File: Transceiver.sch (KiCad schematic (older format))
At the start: 31 parts, among them U2 CC1125, U3 BALF-112X-02D3, U4 SKY13372-467LF, X1 KT2520K40000DAW18TAS

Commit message: project files till workbut names are messed up
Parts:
- C19: footprint (none) -> Capacitors_SMD:C_0201
- C20, C21: footprint (none) -> Capacitors_SMD:C_0402
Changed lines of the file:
@@
 F 0 "C19" V 7550 3800 50  0000 C CNN
 F 1 "47pF" V 7250 3800 50  0000 C CNN
-F 2 "" H 7438 3650 50  0001 C CNN
+F 2 "Capacitors_SMD:C_0201" H 7438 3650 50  0001 C CNN
 F 3 "" H 7400 3800 50  0000 C CNN
 	1    7400 3800
@@
 F 0 "C20" V 9675 3550 50  0000 C CNN
 F 1 "47pF" V 9975 3550 50  0000 C CNN
-F 2 "" H 9863 3400 50  0001 C CNN
+F 2 "Capacitors_SMD:C_0402" H 9863 3400 50  0001 C CNN
 F 3 "" H 9825 3550 50  0000 C CNN
 	1    9825 3550
@@
 F 0 "C21" V 9675 4050 50  0000 C CNN
 F 1 "47pF" V 9975 4050 50  0000 C CNN
-F 2 "" H 9863 3900 50  0001 C CNN
+F 2 "Capacitors_SMD:C_0402" H 9863 3900 50  0001 C CNN
 F 3 "" H 9825 4050 50  0000 C CNN
 	1    9825 4050

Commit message: fixed filesystem
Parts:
- C14: footprint (none) -> Capacitors_SMD:C_0402
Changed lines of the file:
@@
 F 0 "C14" H 4625 3100 50  0000 L CNN
 F 1 "1.8nF" H 4625 2900 50  0000 L CNN
-F 2 "" H 4638 2850 50  0001 C CNN
+F 2 "Capacitors_SMD:C_0402" H 4638 2850 50  0001 C CNN
 F 3 "" H 4600 3000 50  0000 C CNN
 	1    4600 3000

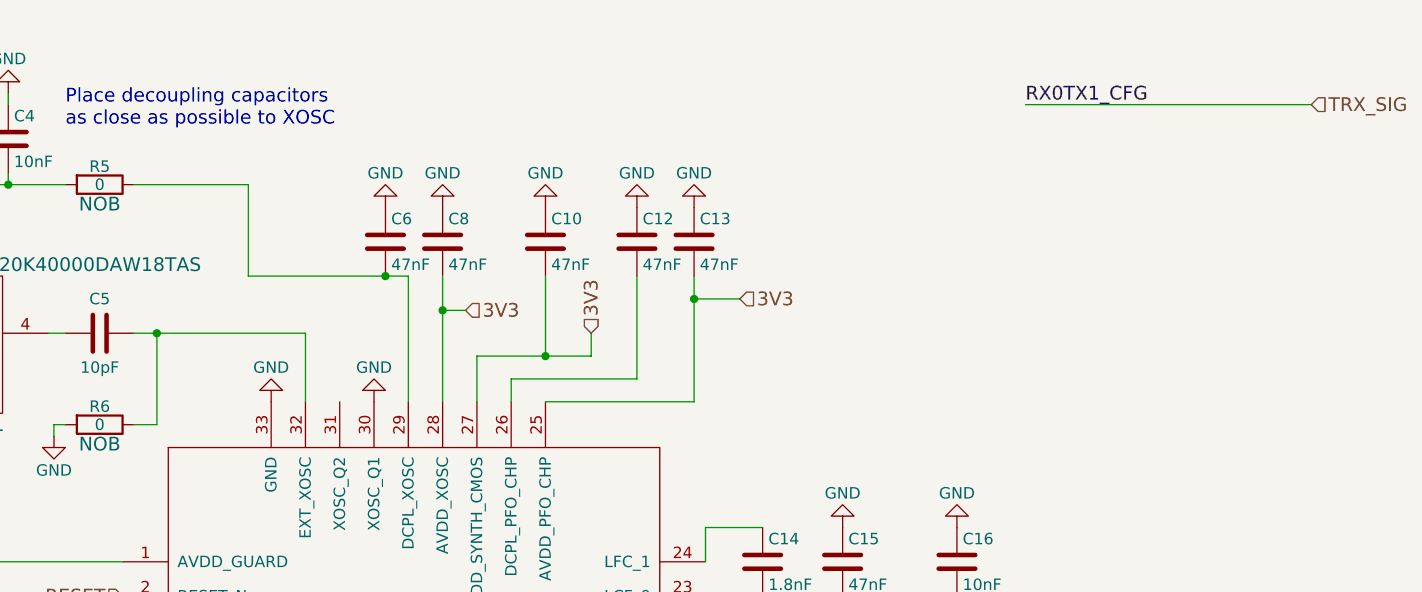
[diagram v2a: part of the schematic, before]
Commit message: added some test points
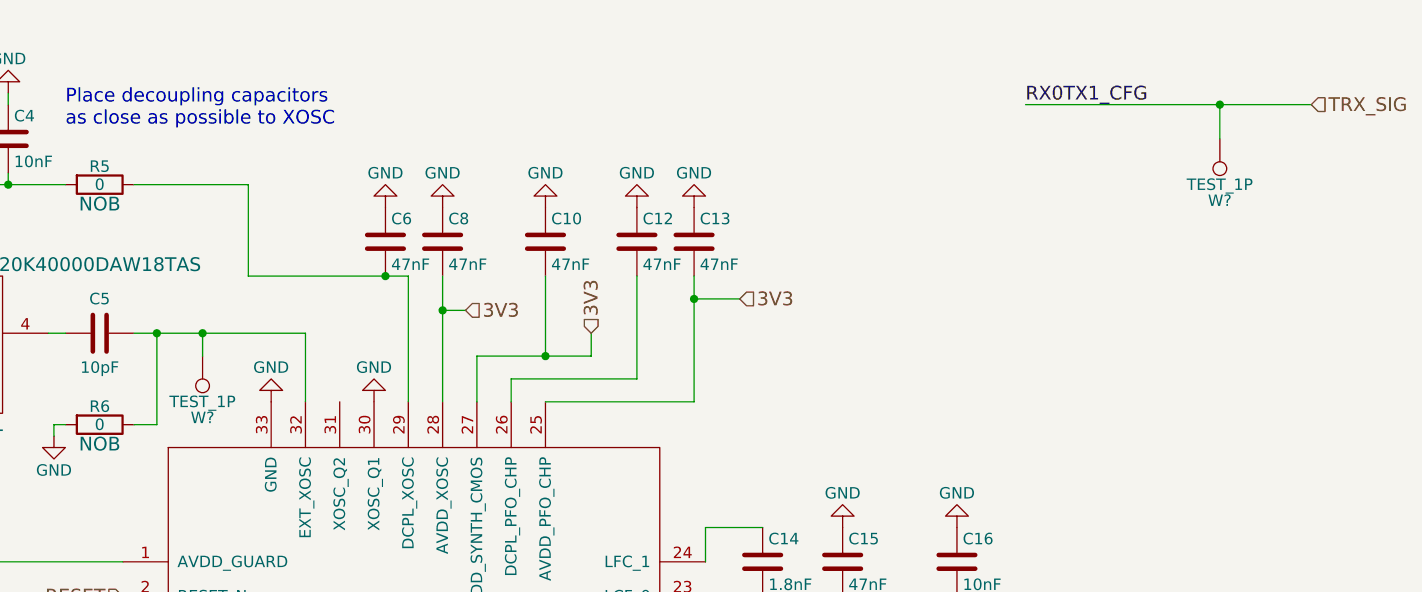
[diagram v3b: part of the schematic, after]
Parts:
- added W? (x2): TEST_1P, symbol TEST_1P
- C19: footprint Capacitors_SMD:C_0201 -> Capacitors_SMD:C_0402
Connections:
- net TRX_SIG: now also W?.1
- net at C5.1, R6.1, U2.32 (EXT_XOSC): now also W?.1
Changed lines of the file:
@@
 F 0 "C19" V 7550 3800 50  0000 C CNN
 F 1 "47pF" V 7250 3800 50  0000 C CNN
-F 2 "Capacitors_SMD:C_0201" H 7438 3650 50  0001 C CNN
+F 2 "Capacitors_SMD:C_0402" H 7438 3650 50  0001 C CNN
 F 3 "" H 7400 3800 50  0000 C CNN
 	1    7400 3800
@@
 Text Label 4800 4050 0    60   ~ 0
 RF_PA
+$Comp
+L TEST_1P W?
+U 1 1 5881B2B5
+P 6600 1150
+F 0 "W?" H 6600 1420 50  0000 C CNN
+F 1 "TEST_1P" H 6600 1350 50  0000 C CNN
+F 2 "" H 6800 1150 50  0000 C CNN
+F 3 "" H 6800 1150 50  0000 C CNN
+	1    6600 1150
+	-1   0    0    1
+$EndComp
+Wire Wire Line
+	6600 1000 6600 1150
+Connection ~ 6600 1000
+$Comp
+L TEST_1P W?
+U 1 1 5881CC09
+P 2150 2100
+F 0 "W?" H 2150 2370 50  0000 C CNN
+F 1 "TEST_1P" H 2150 2300 50  0000 C CNN
+F 2 "" H 2350 2100 50  0000 C CNN
+F 3 "" H 2350 2100 50  0000 C CNN
+	1    2150 2100
+	-1   0    0    1
+$EndComp
+Wire Wire Line
+	2150 2100 2150 2000
+Connection ~ 2150 2000
 $EndSCHEMATC

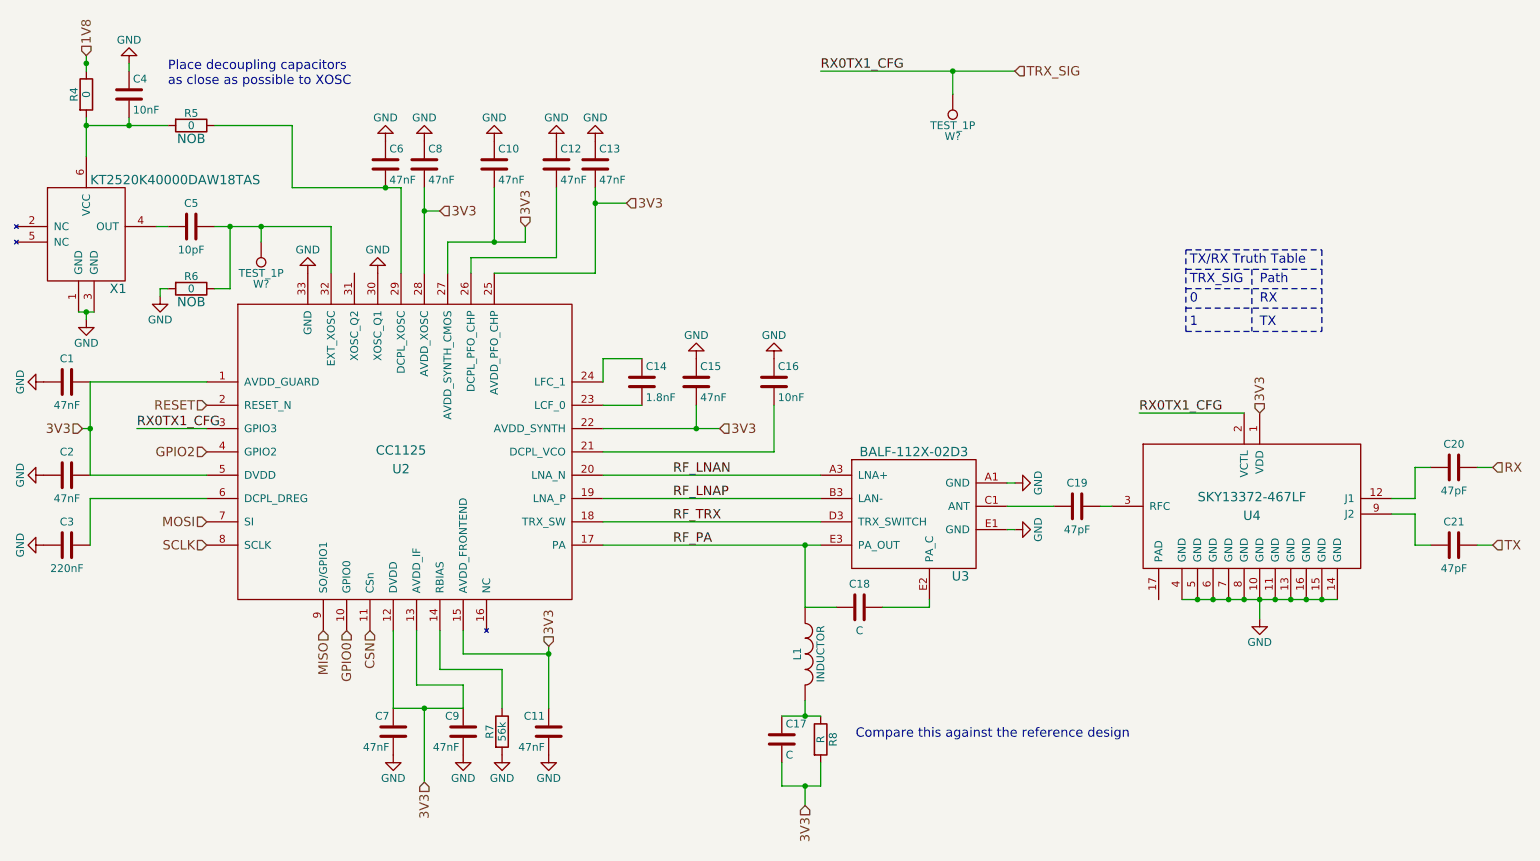
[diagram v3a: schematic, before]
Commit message: layed out all components
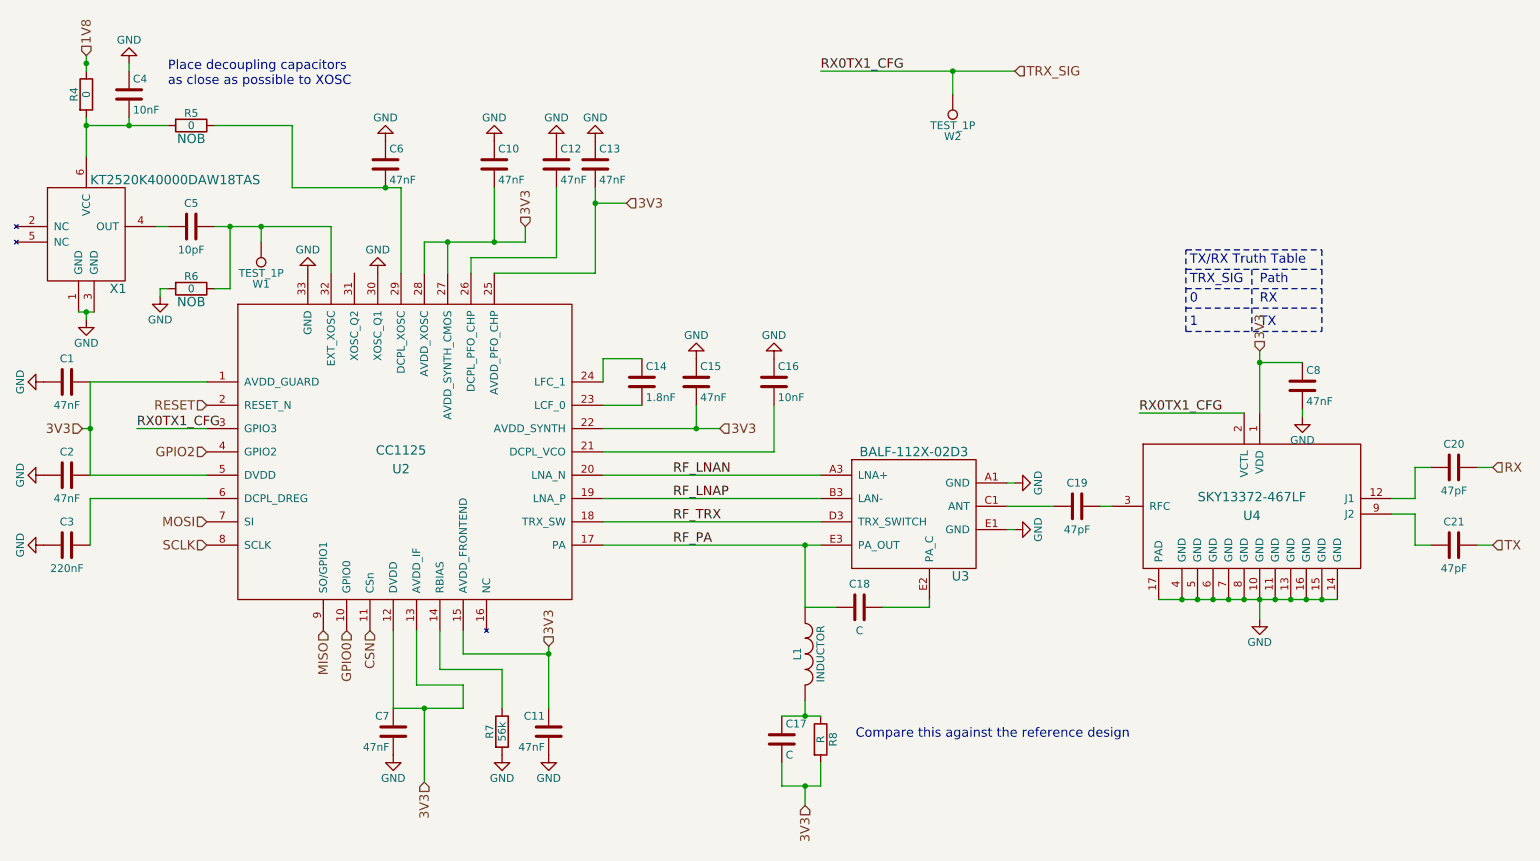
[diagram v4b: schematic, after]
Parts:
- removed C9: 47nF, Capacitors_SMD:C_0402, symbol C
- W1, W2: renamed from W?; footprint (none) -> Measurement_Points:Measurement_Point_Round-SMD-Pad_Small
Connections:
- net 3V3: now also C8.1; no longer C8.2
- net GND: now also C8.2, U4.17 (PAD); no longer C8.1
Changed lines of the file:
@@
-$EndComp
-$Comp
-L C C8
-U 1 1 5821C834
-P 3200 1600
-F 0 "C8" H 3225 1700 50  0000 L CNN
-F 1 "47nF" H 3225 1500 50  0000 L CNN
-F 2 "Capacitors_SMD:C_0402" H 3238 1450 50  0001 C CNN
-F 3 "" H 3200 1600 50  0000 C CNN
-	1    3200 1600
-	1    0    0    -1
-$EndComp
-$Comp
-L GND #PWR09
-U 1 1 5821C83B
-P 3200 1450
-F 0 "#PWR09" H 3200 1200 50  0001 C CNN
-F 1 "GND" H 3200 1300 50  0000 C CNN
-F 2 "" H 3200 1450 50  0000 C CNN
-F 3 "" H 3200 1450 50  0000 C CNN
-	1    3200 1450
-	-1   0    0    1
 $EndComp
 $Comp
@@
 $EndComp
 $Comp
-L GND #PWR010
+L GND #PWR09
 U 1 1 5821C849
 P 3650 1450
-F 0 "#PWR010" H 3650 1200 50  0001 C CNN
+F 0 "#PWR09" H 3650 1200 50  0001 C CNN
 F 1 "GND" H 3650 1300 50  0000 C CNN
 F 2 "" H 3650 1450 50  0000 C CNN
@@
 $EndComp
 $Comp
-L GND #PWR011
+L GND #PWR010
 U 1 1 5821C856
 P 4050 1450
-F 0 "#PWR011" H 4050 1200 50  0001 C CNN
+F 0 "#PWR010" H 4050 1200 50  0001 C CNN
 F 1 "GND" H 4050 1300 50  0000 C CNN
 F 2 "" H 4050 1450 50  0000 C CNN
@@
 $EndComp
 $Comp
-L GND #PWR012
+L GND #PWR011
 U 1 1 5821C863
 P 4300 1450
-F 0 "#PWR012" H 4300 1200 50  0001 C CNN
+F 0 "#PWR011" H 4300 1200 50  0001 C CNN
 F 1 "GND" H 4300 1300 50  0000 C CNN
 F 2 "" H 4300 1450 50  0000 C CNN
@@
 $EndComp
 $Comp
-L GND #PWR013
+L GND #PWR012
 U 1 1 5821C870
 P 2950 1450
-F 0 "#PWR013" H 2950 1200 50  0001 C CNN
+F 0 "#PWR012" H 2950 1200 50  0001 C CNN
 F 1 "GND" H 2950 1300 50  0000 C CNN
 F 2 "" H 2950 1450 50  0000 C CNN
@@
 	1    2950 1450
 	-1   0    0    1
-$EndComp
-$Comp
-L C C9
-U 1 1 5821C876
-P 3450 5250
-F 0 "C9" H 3475 5150 50  0000 L CNN
-F 1 "47nF" H 3475 5350 50  0000 L CNN
-F 2 "Capacitors_SMD:C_0402" H 3488 5100 50  0001 C CNN
-F 3 "" H 3450 5250 50  0000 C CNN
-	1    3450 5250
-	-1   0    0    1
-$EndComp
-$Comp
-L GND #PWR014
-U 1 1 5821C87D
-P 3450 5400
-F 0 "#PWR014" H 3450 5150 50  0001 C CNN
-F 1 "GND" H 3450 5250 50  0000 C CNN
-F 2 "" H 3450 5400 50  0000 C CNN
-F 3 "" H 3450 5400 50  0000 C CNN
-	1    3450 5400
-	1    0    0    -1
 $EndComp
 $Comp
@@
 $EndComp
 $Comp
-L GND #PWR015
+L GND #PWR013
 U 1 1 5821C88A
 P 3000 5400
-F 0 "#PWR015" H 3000 5150 50  0001 C CNN
+F 0 "#PWR013" H 3000 5150 50  0001 C CNN
 F 1 "GND" H 3000 5250 50  0000 C CNN
 F 2 "" H 3000 5400 50  0000 C CNN
@@
 $EndComp
 $Comp
-L GND #PWR016
+L GND #PWR014
 U 1 1 5821C897
 P 4000 5400
-F 0 "#PWR016" H 4000 5150 50  0001 C CNN
+F 0 "#PWR014" H 4000 5150 50  0001 C CNN
 F 1 "GND" H 4000 5250 50  0000 C CNN
 F 2 "" H 4000 5400 50  0000 C CNN
@@
 $EndComp
 $Comp
-L GND #PWR017
+L GND #PWR015
 U 1 1 5821C8A8
 P 3700 5400
-F 0 "#PWR017" H 3700 5150 50  0001 C CNN
+F 0 "#PWR015" H 3700 5150 50  0001 C CNN
 F 1 "GND" H 3700 5250 50  0000 C CNN
 F 2 "" H 3700 5400 50  0000 C CNN
@@
 $EndComp
 $Comp
-L GND #PWR018
+L GND #PWR016
 U 1 1 5821C8BD
 P 4950 2850
-F 0 "#PWR018" H 4950 2600 50  0001 C CNN
+F 0 "#PWR016" H 4950 2600 50  0001 C CNN
 F 1 "GND" H 4950 2700 50  0000 C CNN
 F 2 "" H 4950 2850 50  0000 C CNN
@@
 $EndComp
 $Comp
-L GND #PWR019
+L GND #PWR017
 U 1 1 5821C8CA
 P 5450 2850
-F 0 "#PWR019" H 5450 2600 50  0001 C CNN
+F 0 "#PWR017" H 5450 2600 50  0001 C CNN
 F 1 "GND" H 5450 2700 50  0000 C CNN
 F 2 "" H 5450 2850 50  0000 C CNN
@@
 $EndComp
 $Comp
-L GND #PWR020
+L GND #PWR018
 U 1 1 5821C9D7
 P 2450 2300
-F 0 "#PWR020" H 2450 2050 50  0001 C CNN
+F 0 "#PWR018" H 2450 2050 50  0001 C CNN
 F 1 "GND" H 2450 2150 50  0000 C CNN
 F 2 "" H 2450 2300 50  0000 C CNN
@@
 $EndComp
 $Comp
-L GND #PWR021
+L GND #PWR019
 U 1 1 5821C9E6
 P 2900 2300
-F 0 "#PWR021" H 2900 2050 50  0001 C CNN
+F 0 "#PWR019" H 2900 2050 50  0001 C CNN
 F 1 "GND" H 2900 2150 50  0000 C CNN
 F 2 "" H 2900 2300 50  0000 C CNN
@@
 $EndComp
 $Comp
-L GND #PWR022
+L GND #PWR020
 U 1 1 5821C9FA
 P 1025 2600
-F 0 "#PWR022" H 1025 2350 50  0001 C CNN
+F 0 "#PWR020" H 1025 2350 50  0001 C CNN
 F 1 "GND" H 1025 2450 50  0000 C CNN
 F 2 "" H 1025 2600 50  0000 C CNN
@@
 Text HLabel 1025 900  1    60   Input ~ 0
 1V8
-Text HLabel 3300 1900 2    60   Input ~ 0
-3V3
 Text HLabel 3850 2000 1    60   Input ~ 0
 3V3
@@
 $EndComp
 $Comp
-L GND #PWR023
+L GND #PWR021
 U 1 1 58730157
 P 7000 3650
-F 0 "#PWR023" H 7000 3400 50  0001 C CNN
+F 0 "#PWR021" H 7000 3400 50  0001 C CNN
 F 1 "GND" H 7000 3500 50  0000 C CNN
 F 2 "" H 7000 3650 50  0000 C CNN
@@
 $EndComp
 $Comp
-L GND #PWR024
+L GND #PWR022
 U 1 1 5873019B
 P 7000 3950
-F 0 "#PWR024" H 7000 3700 50  0001 C CNN
+F 0 "#PWR022" H 7000 3700 50  0001 C CNN
 F 1 "GND" H 7000 3800 50  0000 C CNN
 F 2 "" H 7000 3950 50  0000 C CNN
@@
 Text Notes 1550 1100 0    60   ~ 0
 Place decoupling capacitors\nas close as possible to XOSC\n
-Text HLabel 8575 3200 1    60   Input ~ 0
+Text HLabel 8575 2800 1    60   Input ~ 0
 3V3
 $Comp
@@
 	3350 2300 3350 2100
 Wire Wire Line
-	3350 2100 3850 2100
+	3200 2100 3850 2100
 Wire Wire Line
 	3650 2100 3650 1750
@@
 	3850 2100 3850 2000
 Connection ~ 3650 2100
-Wire Wire Line
-	3200 1750 3200 2300
-Wire Wire Line
-	3200 1900 3300 1900
-Connection ~ 3200 1900
 Wire Wire Line
 	3050 1750 3050 2300
@@
 	8525 2275 8525 2675
 $Comp
-L GND #PWR025
+L GND #PWR023
 U 1 1 58748992
 P 8575 4525
-F 0 "#PWR025" H 8575 4275 50  0001 C CNN
+F 0 "#PWR023" H 8575 4275 50  0001 C CNN
 F 1 "GND" H 8575 4375 50  0000 C CNN
 F 2 "" H 8575 4525 50  0000 C CNN
@@
 $EndComp
 Wire Wire Line
-	8075 4400 9075 4400
+	7925 4400 9075 4400
 Connection ~ 8175 4400
 Connection ~ 8275 4400
@@
 	1300 1300 1300 1350
 $Comp
-L GND #PWR026
+L GND #PWR024
 U 1 1 5873A98A
 P 1300 950
-F 0 "#PWR026" H 1300 700 50  0001 C CNN
+F 0 "#PWR024" H 1300 700 50  0001 C CNN
 F 1 "GND" H 1300 800 50  0000 C CNN
 F 2 "" H 1300 950 50  0000 C CNN
@@
 	1500 2400 1500 2450
 $Comp
-L GND #PWR027
+L GND #PWR025
 U 1 1 5873E01A
 P 1500 2450
-F 0 "#PWR027" H 1500 2200 50  0001 C CNN
+F 0 "#PWR025" H 1500 2200 50  0001 C CNN
 F 1 "GND" H 1500 2300 50  0000 C CNN
 F 2 "" H 1500 2450 50  0000 C CNN
@@
 RF_PA
 $Comp
-L TEST_1P W?
+L TEST_1P W2
 U 1 1 5881B2B5
 P 6600 1150
-F 0 "W?" H 6600 1420 50  0000 C CNN
+F 0 "W2" H 6600 1420 50  0000 C CNN
 F 1 "TEST_1P" H 6600 1350 50  0000 C CNN
-F 2 "" H 6800 1150 50  0000 C CNN
+F 2 "Measurement_Points:Measurement_Point_Round-SMD-Pad_Small" H 6800 1150 50  0001 C CNN
 F 3 "" H 6800 1150 50  0000 C CNN
 	1    6600 1150
@@
 Connection ~ 6600 1000
 $Comp
-L TEST_1P W?
+L TEST_1P W1
 U 1 1 5881CC09
 P 2150 2100
-F 0 "W?" H 2150 2370 50  0000 C CNN
+F 0 "W1" H 2150 2370 50  0000 C CNN
 F 1 "TEST_1P" H 2150 2300 50  0000 C CNN
-F 2 "" H 2350 2100 50  0000 C CNN
+F 2 "Measurement_Points:Measurement_Point_Round-SMD-Pad_Small" H 2350 2100 50  0001 C CNN
 F 3 "" H 2350 2100 50  0000 C CNN
 	1    2150 2100
@@
 	2150 2100 2150 2000
 Connection ~ 2150 2000
+Wire Wire Line
+	3200 2300 3200 2100
+Connection ~ 3350 2100
+$Comp
+L C C8
+U 1 1 58834AA4
+P 8850 3025
+F 0 "C8" H 8875 3125 50  0000 L CNN
+F 1 "47nF" H 8875 2925 50  0000 L CNN
+F 2 "Capacitors_SMD:C_0402" H 8888 2875 50  0001 C CNN
+F 3 "" H 8850 3025 50  0000 C CNN
+	1    8850 3025
+	1    0    0    -1
+$EndComp
+$Comp
+L GND #PWR026
+U 1 1 5883AD14
+P 8850 3225
+F 0 "#PWR026" H 8850 2975 50  0001 C CNN
+F 1 "GND" H 8850 3075 50  0000 C CNN
+F 2 "" H 8850 3225 50  0000 C CNN
+F 3 "" H 8850 3225 50  0000 C CNN
+	1    8850 3225
+	1    0    0    -1
+$EndComp
+Wire Wire Line
+	8575 2800 8575 3200
+Wire Wire Line
+	8850 2875 8575 2875
+Connection ~ 8575 2875
+Wire Wire Line
+	8850 3175 8850 3225
+Connection ~ 8075 4400
 $EndSCHEMATC

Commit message: continued routing
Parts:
- removed R4, R5, R6: 0, Resistors_SMD:R_0402, symbol R
- C4: value 10nF -> 100nF
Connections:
- net 1V8: now also C4.2, X1.6 (VCC)
